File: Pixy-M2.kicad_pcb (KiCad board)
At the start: 4 copper layers, 66 x 100 mm, 78 parts, among them J1 USB_C_Receptacle_USB2.0_14P, J10 SM09B-SRSS-TB, J11 SM06B-SRSS-TB, J4 SM06B-SRSS-TB, J5 SM06B-SRSS-TB, J6 SM06B-SRSS-TB, J7 SM06B-SRSS-TB, J8 SM06B-SRSS-TB, J9 SM06B-SRSS-TB, Q1 AO4407A, SW1 SW_Push, SW2 SW_Push, SW3 JS102011SAQN, U1 ESP32-S3-WROOM-1-N16, U2 USBLC6-2SC6, U3 AP63203WU, U4 DRV8231ADSG, U5 DRV8231ADSG

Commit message: silkscreen: mark the battery bay and its lead route
B.SilkS now shows where the pack goes:
- its 62 x 17 mm outline between the motors, labelled with the part
  and "62 x 17 face on board, hook-and-loop";
- an arrow at the +X end where the XT30 and balance leads leave;
- the lead route as a dashed line forward and across the front strip,
  ending in an arrow at the left edge beside BT1's pins.

Each motor's "Pololu HP 6V N20" label used to sit in the inboard
encoder allowance, which is now inside the battery outline. The labels
move to the outboard allowance, and "ENC CONN SIDE" marks the face the
encoder board stands proud of.

battery_bay.py prints the battery marks, and assembly_marks.py draws the
motor labels in their new place. Run standalone, battery_bay.py moves
the labels on an already-marked board. A full rework.py regeneration
reproduces the board item for item. DRC is 0 violations, 0 unconnected
and 0 parity issues. The aperture audit passes. docs/images/
pcb-3d-bottom.png is re-rendered.

Co-Authored-By: Claude Opus 5.5 <noreply@anthropic.com>
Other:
- board text added: "62 x 17 face on board, hook-and-loop"
- board text added: "BATTERY 2S LiPo 450 mAh"
- board text added: "ENC CONN SIDE"
- board text added: "XT30 + balance leads"
- board text added: "XT30 LEAD: ROUND LEFT EDGE TO BT1 (TOP)"
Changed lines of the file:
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@@
 	)
 	(gr_line
+		(start 100.5 117.5)
+		(end 162.5 117.5)
+		(stroke
+			(width 0.15)
+			(type solid)
+		)
+		(layer "B.SilkS")
+	)
+	(gr_line
+		(start 100.5 134.5)
+		(end 100.5 117.5)
+		(stroke
+			(width 0.15)
+			(type solid)
+		)
+		(layer "B.SilkS")
+	)
+	(gr_line
+		(start 100.8 89.5)
+		(end 101.4928 89.1)
+		(stroke
+			(width 0.15)
+			(type solid)
+		)
+		(layer "B.SilkS")
+	)
+	(gr_line
+		(start 100.8 89.5)
+		(end 101.4928 89.9)
+		(stroke
+			(width 0.15)
+			(type solid)
+		)
+		(layer "B.SilkS")
+	)
+	(gr_line
 		(start 100.8 112.5)
 		(end 101.4928 112.1)
@@
 	)
 	(gr_line
+		(start 102.8 89.5)
+		(end 100.8 89.5)
+		(stroke
+			(width 0.15)
+			(type solid)
+		)
+		(layer "B.SilkS")
+	)
+	(gr_line
 		(start 106 112.5)
 		(end 100.8 112.5)
@@
 	)
 	(gr_line
+		(start 156 126)
+		(end 162.2 126)
+		(stroke
+			(width 0.15)
+			(type solid)
+		)
+		(layer "B.SilkS")
+	)
+	(gr_line
 		(start 157 136)
 		(end 157 148)
@@
 	)
 	(gr_line
+		(start 162.2 126)
+		(end 161.5072 125.6)
+		(stroke
+			(width 0.15)
+			(type solid)
+		)
+		(layer "B.SilkS")
+	)
+	(gr_line
+		(start 162.2 126)
+		(end 161.5072 126.4)
+		(stroke
+			(width 0.15)
+			(type solid)
+		)
+		(layer "B.SilkS")
+	)
+	(gr_line
+		(start 162.5 117.5)
+		(end 162.5 134.5)
+		(stroke
+			(width 0.15)
+			(type solid)
+		)
+		(layer "B.SilkS")
+	)
+	(gr_line
+		(start 162.5 126)
+		(end 164.5 124)
+		(stroke
+			(width 0.15)
+			(type dash)
+		)
+		(layer "B.SilkS")
+	)
+	(gr_line
+		(start 162.5 134.5)
+		(end 100.5 134.5)
+		(stroke
+			(width 0.15)
+			(type solid)
+		)
+		(layer "B.SilkS")
+	)
+	(gr_line
+		(start 164.5 89.5)
+		(end 100.8 89.5)
+		(stroke
+			(width 0.15)
+			(type dash)
+		)
+		(layer "B.SilkS")
+	)
+	(gr_line
+		(start 164.5 124)
+		(end 164.5 89.5)
+		(stroke
+			(width 0.15)
+			(type dash)
+		)
+		(layer "B.SilkS")
+	)
+	(gr_line
 		(start 165.2 144.5)
 		(end 164.5072 144.1)
@@
 	)
 	(gr_text "Pololu HP 6V N20"
-		(at 116 118 0)
+		(at 112 102 0)
 		(layer "B.SilkS")
 		(effects
@@
 		)
 	)
+	(gr_text "ENC CONN SIDE"
+		(at 128 102 0)
+		(layer "B.SilkS")
+		(effects
+			(font
+				(size 1 1)
+				(thickness 0.15)
+			)
+			(justify mirror)
+		)
+	)
 	(gr_text "ENC"
 		(at 128 110 0)
@@
 		)
 	)
+	(gr_text "BATTERY  2S LiPo 450 mAh"
+		(at 131.5 121 0)
+		(layer "B.SilkS")
+		(effects
+			(font
+				(size 1 1)
+				(thickness 0.15)
+			)
+			(justify mirror)
+		)
+	)
+	(gr_text "62 x 17 face on board, hook-and-loop"
+		(at 131.5 123.5 0)
+		(layer "B.SilkS")
+		(effects
+			(font
+				(size 1 1)
+				(thickness 0.15)
+			)
+			(justify mirror)
+		)
+	)
+	(gr_text "XT30 LEAD: ROUND LEFT EDGE TO BT1 (TOP)"
+		(at 132 88 0)
+		(layer "B.SilkS")
+		(effects
+			(font
+				(size 1 1)
+				(thickness 0.15)
+			)
+			(justify mirror)
+		)
+	)
 	(gr_text "ENC"
 		(at 138 142 0)
@@
 		)
 	)
+	(gr_text "ENC CONN SIDE"
+		(at 138 150 0)
+		(layer "B.SilkS")
+		(effects
+			(font
+				(size 1 1)
+				(thickness 0.15)
+			)
+			(justify mirror)
+		)
+	)
 	(gr_text "MOTOR B"
 		(at 149.5 140.5 0)
@@
 		)
 	)
+	(gr_text "XT30 + balance leads"
+		(at 151 128.5 0)
+		(layer "B.SilkS")
+		(effects
+			(font
+				(size 1 1)
+				(thickness 0.15)
+			)
+			(justify mirror)
+		)
+	)
 	(gr_text "Pololu HP 6V N20"
-		(at 150 134 0)
+		(at 154 150 0)
 		(layer "B.SilkS")
 		(effects
@@
 	(group "MOTOR A left"
 		(members "182aea95-9cac-46fa-9891-7ba377806479" "2f65c22c-14ae-4f42-a709-9b8d5caaa5b2"
-			"724801b8-62fc-4983-98b0-ae9173e109c6" "731f0e17-fc26-4354-be69-66f241ecec50"
-			"78fb0ae1-b412-4b57-b170-880f7e821dcf" "8c104fb5-1e0c-45c4-922a-1d16e56ce52a"
-			"932dff99-57df-49bd-b39b-bcbb18650a0f" "96fded54-0e83-4a2c-af15-2bd8b529ef9e"
-			"9f73eaea-9302-4c33-ad8d-0effa9570fa8" "9fbd5650-8a3e-4572-a359-2861bb6658ff"
-			"a19da8c7-bf97-4091-8b3c-38a013214ff2" "b732a7a5-04e5-43d0-b666-8b87410bfe6f"
-			"b8f2ee2f-2cc3-4c76-8a9d-eeb49646817c" "ef057167-08ec-4e79-9cf7-0bf9724b438e"
+			"53c676fe-a335-40a2-9a87-d7526bc6f8c1" "724801b8-62fc-4983-98b0-ae9173e109c6"
+			"731f0e17-fc26-4354-be69-66f241ecec50" "78fb0ae1-b412-4b57-b170-880f7e821dcf"
+			"8c104fb5-1e0c-45c4-922a-1d16e56ce52a" "932dff99-57df-49bd-b39b-bcbb18650a0f"
+			"96fded54-0e83-4a2c-af15-2bd8b529ef9e" "9f73eaea-9302-4c33-ad8d-0effa9570fa8"
+			"9fbd5650-8a3e-4572-a359-2861bb6658ff" "a19da8c7-bf97-4091-8b3c-38a013214ff2"
+			"b732a7a5-04e5-43d0-b666-8b87410bfe6f" "b8f2ee2f-2cc3-4c76-8a9d-eeb49646817c"
+			"ef057167-08ec-4e79-9cf7-0bf9724b438e"
 		)
 	)
 	(group "MOTOR B right"
 		(members "0f1f0ffd-d82d-4e67-a17a-63341daef4a0" "0fdc3546-4d59-47d1-8cc6-e377abaa7ab5"
-			"4a79a600-30c0-4714-a8a7-72aed6312c1c" "7daca688-97f0-4970-939d-d535cb80d69c"
-			"8e764ac1-cf16-446e-a34d-87ffc74df771" "a9721b52-0e68-417a-8dd7-89f1f280f427"
-			"ad33dd5f-4225-4708-816f-030241213b0d" "b8e69d41-da5b-42cb-b5ad-6211be34cdf2"
-			"bcda8ce7-7330-4a6e-ad1a-35d33d416d2b" "d6442bf3-5cec-4718-aa87-49ee13f4cb53"
-			"d6f641c7-7735-4c2b-8e4d-9783522e7b47" "efc585e6-88f0-4ecc-bb5d-9bfebf6fc967"
-			"f00c8229-d97d-464d-8c04-33f36ac6bb3d" "f21dc9e0-eb5e-45dd-a607-3d5a687f84eb"
+			"4912f350-1b29-4300-95c6-d19ba006e40e" "4a79a600-30c0-4714-a8a7-72aed6312c1c"
+			"7daca688-97f0-4970-939d-d535cb80d69c" "8e764ac1-cf16-446e-a34d-87ffc74df771"
+			"a9721b52-0e68-417a-8dd7-89f1f280f427" "ad33dd5f-4225-4708-816f-030241213b0d"
+			"b8e69d41-da5b-42cb-b5ad-6211be34cdf2" "bcda8ce7-7330-4a6e-ad1a-35d33d416d2b"
+			"d6442bf3-5cec-4718-aa87-49ee13f4cb53" "d6f641c7-7735-4c2b-8e4d-9783522e7b47"
+			"efc585e6-88f0-4ecc-bb5d-9bfebf6fc967" "f00c8229-d97d-464d-8c04-33f36ac6bb3d"
+			"f21dc9e0-eb5e-45dd-a607-3d5a687f84eb"
+		)
+	)
+	(group "Battery 2S LiPo"
+		(members "1f756f54-700a-4b72-8c48-fb78f77be5c2" "2bf49ae5-ad71-47fd-bcae-bb4a34affefd"
+			"2e12e2d9-c110-41b5-a665-7e36aaf4e661" "30fa4877-ac52-4ba0-802d-24a011503e21"
+			"42349a8b-0c73-4b39-a33c-f898558e7e66" "58017f5e-8cc7-438d-83ad-afd2513fb6b0"
+			"5a2f327a-d665-4a46-a37a-faead681c1b4" "67de89d8-07e8-459d-9cf0-97794442ad0c"
+			"705298cb-41fb-4b0a-b5c3-0a6fb6671598" "70fec421-3e8d-4c27-af04-3baa416c8687"
+			"8010a8b4-c589-4faa-9333-068803a2f652" "92ea9e6d-a648-4d3e-b0e9-235c1ea28ac4"
+			"a3650a10-ee04-4e65-a642-60867b826b2a" "b819c550-9660-4e89-8e2f-7ab50507bc72"
+			"e30f7bb5-e967-4b4e-8e8a-673eae03dd72" "ead91f8e-c96c-49e1-886a-5d0ad5f9b5c2"
+			"efb92332-e236-4b47-93ee-39151fe97e23"
 		)
 	)

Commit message: layout: move R8/C13 beside U3.2 and take REG_EN out from under U3
REG_EN is a ~20 kOhm node 1.2 V above the EN comparator threshold, and
the layout rule was to put R8 and C13 next to U3.2. The issue-5 FB trace
ran down U3's west side, so EN could only leave through a via under the
package, 0.40 mm from the SW pin. R8 and C13 sat 7.35 and 9.9 mm of
copper away.

C13 and R8 now stand in a row just west of U3, and EN -> C13.1 -> R8.1
is one straight top-layer run (1.91 / 3.66 mm of copper). FB keeps its
via-free top-layer sense to C11 and turns south round the outside of the
new parts. A via on FB would bond it to the In2 3V3 pour beside U3,
which is what review finding 5 removed. REG_EN's long leg crosses under
FB on B.Cu instead; both of its vias are 5.65 mm or more from switching
copper. The VSYS hop's upper via moves north of FB. New vias keep their
In1/In2 antipads separate.

REG_EN's closest approach to SW/BST is now U3's own 0.95 mm pin gap, and
the "REG_EN clear of the switch node" floor goes from 0.35 to 0.9 mm. It
fires on the old board and on a copy with REG_EN copper under U3.

tools/autoroute/reg_en.py does this, and rework.py runs it last. A full
rework.py regeneration reproduces the board item for item. DRC is 0
violations, 0 unconnected and 0 parity issues; the aperture audit passes
with 253 vias. Evidence is in layout/reg-en/.

Also corrects issue 5's note that FB stays 2.1 mm from SW/BST: it passes
TP4 at 1.35 mm, before and after this change. docs/images/pcb-3d-top.png
and pcb-copper-top.png are re-rendered; pcb-3d-iso.png is not, since its
camera settings are not recorded.

Co-Authored-By: Claude Opus 5.5 <noreply@anthropic.com>
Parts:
- moved C13 6.06 mm to (136.2, 97.0), turned to -90 degrees
- moved R8 4.03 mm to (134.5, 97.2), turned to -90 degrees
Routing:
- net /ESP_3V3: track 93.8 -> 102.0 mm
- net /REG_EN: track 17.7 -> 14.3 mm
- net /VSYS: track 37.2 -> 37.8 mm
- net GND: track 114.9 -> 115.4 mm

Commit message: layout: keep the IPROPI sense runs clear of motor and drive copper
GPIO2 and GPIO10 carry each DRV8231A's IPROPI output (1500 uA/A into
2.2 kOhm) to the ADC. They came within 0.70 mm (GPIO2, MOT_A_1 at J8) and
0.53 mm (GPIO10, MOT_A_2) of motor copper, and ran long stretches beside
their own driver's IN1/IN2. The cause was where the sense resistors sat:

- R17 was east of U4's IN1/IN2 escapes, so GPIO2 hopped over them on
  B.Cu over the In2 VBAT island. But the three nets leave U4 in the order
  they reach U1's west column, so nothing else needed that crossing.
- R18 was west of U5's stacked GPIO41/42 pair, so GPIO10 ran down the
  channel beside MOT_A_2, then 8 mm beside GPIO42 on B.Cu at 0.25 mm.

R17 moves west of the escapes and GPIO2 runs down beside it, 1.7 mm from
MOT_A_1, with no via. R18 moves east of the pair. GPIO10 crosses the pair
once, under U5's own pins, then rises to R18 and rejoins its old diagonal
to U1 past the island. The channel beside MOT_A_2 is left empty.

GPIO2/GPIO10 now come no closer than 1.30 / 0.80 mm to motor copper: U4's
own pin 1 to pin 8, and GPIO10's escape via. No other stretch is within
1 mm. Track within 0.6 mm of a drive line falls from 6.8 / 13.7 mm to
3.7 / 5.6 mm. The "IPROPI clear of motor outputs" floor goes from 0.25
to 0.75 mm, and fires on the old board and on a broken copy.

tools/autoroute/ipropi.py does this, and rework.py runs it after
reg_en.py. A full rework.py regeneration reproduces the board item for
item. DRC is 0 violations, 0 unconnected and 0 parity issues, and ERC is
0. The aperture audit passes with 254 vias. Evidence is in layout/ipropi/.

The README item now asks only for the hardware check. TI's remedy for
early current-limit trips, 10 nF on IPROPI, can be stacked on R17/R18.
The firmware notes add that IPROPI reads nothing in coast.
docs/images/pcb-3d-top.png and pcb-copper-top.png are re-rendered.

Co-Authored-By: Claude Opus 5.5 <noreply@anthropic.com>
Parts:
- moved R17 5.05 mm to (104.5, 120.3), turned to 90 degrees
- moved R18 2.57 mm to (118.5, 118.6), turned to 180 degrees
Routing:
- net /GPIO10: track 42.7 -> 38.6 mm, vias 2 -> 4
- net /GPIO2: track 53.5 -> 51.6 mm, vias 2 -> 0
- net GND: track 115.4 -> 115.6 mm, vias 88 -> 89

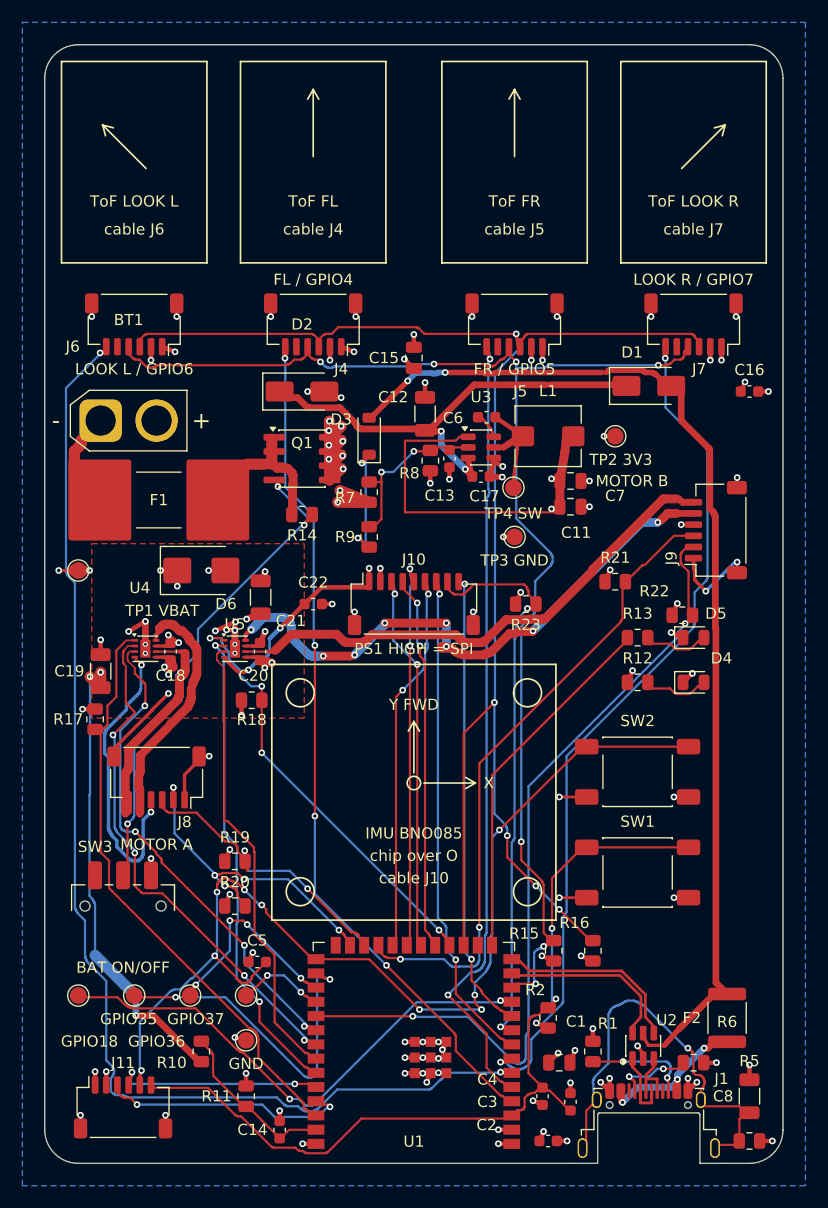
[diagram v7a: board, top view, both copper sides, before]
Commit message: U1: plug-in ESP32-S3-DevKitC-1-N8R8 on SMD sockets, same 66 x 100 mm board
Replace the soldered WROOM-1 module with an Espressif ESP32-S3-DevKitC-1-N8R8
(v1.1) on two 1x22 2.54 mm SMD female headers, and remove what the devkit
carries itself. The outline stays 66 x 100 mm for the diagonal runs.

Schematic (tools/schematic/devkit.py):
- U1 -> PCM_Espressif:ESP32-S3-DevKitC on Pixy-M2:ESP32-S3-DevKitC-1_SMD_Sockets;
  Value, Footprint, Datasheet and MPN changed together.
- 21 parts removed: the USB-C input (J1, U2, F2, R1, R5, R6, C8), the USB
  supply path (D1, D3, R9), reset/boot (R2, C3-C5, SW1, SW2), J11 and TP5-TP8.
- The AP63203 feeds the devkit's 3V3 pins; its 5V pin is unused.
- Encoder B OUT B moves from GPIO38 (the v1.1 RGB LED) to GPIO18.
- 13 no-connect flags on the pins the devkit uses itself. 59 nets, 57 parts,
  ERC 0/0.

Layout (tools/autoroute/devkit.py, new rework stage 20):
- U1 along the right edge, antenna over the rear edge, USB end to the front.
- The IMU moves into the 25 mm column beside the devkit (8.6 mm left of and
  7.5 mm behind the rotation centre). J10/C22 go behind it, J8/SW3 clear of
  it, J9 in front of the devkit, the LEDs to the rear-left corner and the
  sense chain against GPIO1.
- Rips and re-routes every affected net, keeping the hand-placed motor-corner,
  buck, FB and REG_EN copper. A* respects the custom clearance floors. The
  stage ends with KiCad-style dead-end pruning, removal of via-only GND stubs
  and one GND via per B.Cu pour island.
- Closes J1's outline notch and moves the antenna keep-out.
- Footprint generator: tools/autoroute/devkit_footprint.py.
- DRC 0 violations / 0 unconnected / 0 parity. Aperture audit passes with
  192 vias (254 on main). A full rework.py replay reproduces the board.
- Measurements are in layout/devkit/. Motor loops: A 26.4 mm², B 27.8 mm²
  (main 23.9 / 9.8, where B's opposite lobes nearly cancelled).

Rules: USB rules and netclass removed; Hole clearance 0.30 mm everywhere.
via_openings.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
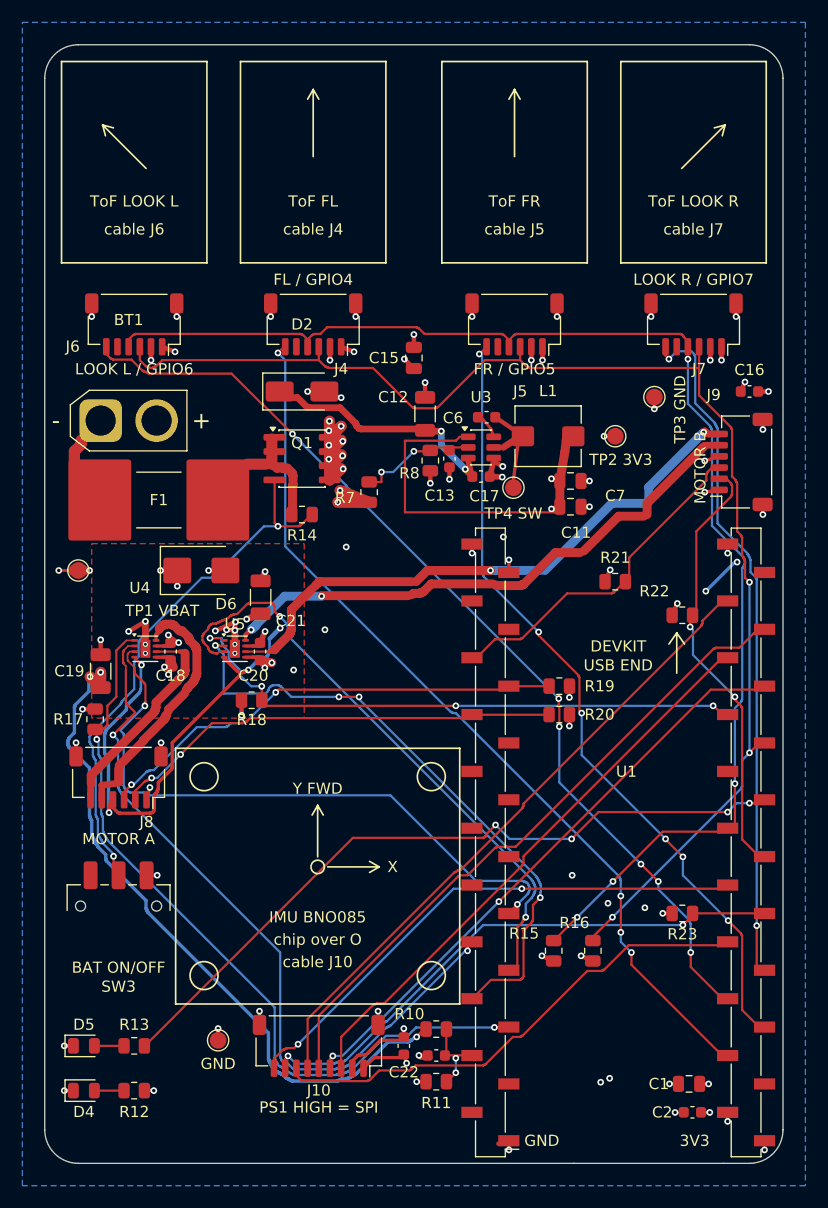
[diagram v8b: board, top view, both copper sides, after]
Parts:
- removed C3: 1uF 16V, Capacitor_SMD:C_0603_1608Metric
- removed C4, C5: 0.1uF 16V, Capacitor_SMD:C_0603_1608Metric
- removed C8: 4.7nF 1kV, Capacitor_SMD:C_1206_3216Metric
- removed D1: MBRA340T3G, Diode_SMD:D_SMA
- removed D3: BAT54W, Diode_SMD:D_SOD-123
- removed F2: 500mA 15V, Fuse:Fuse_1812_4532Metric
- removed J1: USB_C_Receptacle_USB2.0_14P, Connector_USB:USB_C_Receptacle_Amphenol_12401948E412A
- removed J11: SM06B-SRSS-TB, Connector_JST:JST_SH_SM06B-SRSS-TB_1x06-1MP_P1.00mm_Horizontal
- removed R1, R6: 5.1kOhm, Resistor_SMD:R_0805_2012Metric
- removed R2: 10kOhm, Resistor_SMD:R_0805_2012Metric
- removed R5: 1MOhm, Resistor_SMD:R_0805_2012Metric
- removed R9: 39kOhm 1%, Resistor_SMD:R_0805_2012Metric
- removed SW1, SW2: SW_Push, Button_Switch_SMD:SW_Push_1P1T_NO_E-Switch_TL3301NxxxxxG
- removed TP5: GPIO18, TestPoint:TestPoint_Pad_D1.5mm
- removed TP6: GPIO35, TestPoint:TestPoint_Pad_D1.5mm
- removed TP7: GPIO36, TestPoint:TestPoint_Pad_D1.5mm
- removed TP8: GPIO37, TestPoint:TestPoint_Pad_D1.5mm
- removed U2: USBLC6-2SC6, Package_TO_SOT_SMD:SOT-23-6
- U1: value ESP32-S3-WROOM-1-N16 -> ESP32-S3-DevKitC-1-N8R8; footprint Pixy-M2:ESP32-S3-WROOM-1_AntennaOverhang -> Pixy-M2:ESP32-S3-DevKitC-1_SMD_Sockets
- moved D4 65.6 mm to (103.5, 153.5)
- moved D5 65.6 mm to (103.5, 149.5)
- moved R12 57.9 mm to (108.0, 153.5), turned to 180 degrees
- moved R13 57.9 mm to (108.0, 149.5), turned to 180 degrees
- moved J10 40.4 mm to (124.5, 149.5), turned to 180 degrees
- moved C22 40.3 mm to (132.1, 149.5), turned to 90 degrees
- moved R20 33.7 mm to (146.0, 119.9), turned to 180 degrees
- moved R19 33.0 mm to (146.0, 117.3), turned to 180 degrees
- moved R23 31.0 mm to (157.0, 137.7)
- moved U1 30.8 mm to (162.7, 158.0)
- moved R10 21.1 mm to (135.0, 148.0), turned to 0 degrees
- moved TP3 17.7 mm to (154.5, 91.5)
- moved R11 17.0 mm to (135.0, 152.7), turned to 180 degrees
- moved C14 15.5 mm to (135.0, 150.4), turned to 180 degrees
- moved C2 13.2 mm to (157.9, 155.4), turned to 180 degrees
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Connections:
- J9 pad 2: /GPIO38 -> /GPIO18
- R22 pad 2: /GPIO38 -> /GPIO18
- U1 pad 1: GND -> /ESP_3V3
- U1 pad 13: /USB_D- -> /GPIO3
- U1 pad 14: /USB_D+ -> unconnected-(U1-GPIO46-Pad14)
- U1 pad 15: /GPIO3 -> /GPIO9
- U1 pad 16: unconnected-(U1-GPIO46-Pad16) -> /GPIO10
- U1 pad 17: /GPIO9 -> /GPIO11
- U1 pad 18: /GPIO10 -> /GPIO12
- U1 pad 19: /GPIO11 -> /GPIO13
- U1 pad 20: /GPIO12 -> /GPIO14
- U1 pad 21: /GPIO13 -> unconnected-(U1-5V-Pad21)
- U1 pad 22: /GPIO14 -> GND
- U1 pad 23: /GPIO21 -> GND
- U1 pad 24: /GPIO47 -> GND
- U1 pad 25: /GPIO48 -> unconnected-(U1-GPIO19/USB_D--Pad25)
- U1 pad 27: /GPIO0 -> /GPIO21
- U1 pad 28: /GPIO35 -> /GPIO47
- U1 pad 29: /GPIO36 -> /GPIO48
- U1 pad 3: /CHIP_PU -> unconnected-(U1-CHIP_PU-Pad3)
- U1 pad 30: /GPIO37 -> unconnected-(U1-GPIO45-Pad30)
- U1 pad 31: /GPIO38 -> unconnected-(U1-GPIO0-Pad31)
- U1 pad 32: /GPIO39 -> unconnected-(U1-GPIO35-Pad32)
- U1 pad 33: /GPIO40 -> unconnected-(U1-GPIO36-Pad33)
- U1 pad 34: /GPIO41 -> unconnected-(U1-GPIO37-Pad34)
- U1 pad 35: /GPIO42 -> unconnected-(U1-GPIO38-Pad35)
- U1 pad 36: /GPIO44 -> /GPIO39
- U1 pad 37: /GPIO43 -> /GPIO40
- U1 pad 38: /GPIO2 -> /GPIO41
- U1 pad 39: /VBAT_SENSE -> /GPIO42
- U1 pad 40: GND -> /GPIO2
- U1 pad 41: GND -> /VBAT_SENSE
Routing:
- net /VBUS: track 90.4 -> 0.00 mm, vias 2 -> 0
- net /GPIO0: track 89.8 -> 0.00 mm, vias 9 -> 0
- net /GPIO38: track 71.7 -> 0.00 mm, vias 2 -> 0
- net /CHIP_PU: track 71.4 -> 0.00 mm, vias 2 -> 0
- net GND: track 115.6 -> 75.9 mm, vias 89 -> 72
- net /GPIO3: track 31.2 -> 64.3 mm, vias 0 -> 4
- net Net-(J1-SHIELD): track 32.3 -> 0.00 mm, vias 1 -> 0
- net /GPIO35: track 30.0 -> 0.00 mm, vias 2 -> 0
- net /GPIO21: track 55.0 -> 27.9 mm, vias 2 -> 0
- net /GPIO13: track 34.6 -> 57.3 mm, vias 2 -> 0
- net /GPIO6: track 107.5 -> 85.7 mm, vias 2 -> 6
- net /GPIO14: track 34.6 -> 56.3 mm, vias 2 -> 0
- net /GPIO43: track 21.1 -> 0.00 mm, vias 2 -> 0
- net /GPIO40: track 46.3 -> 66.9 mm, vias 4 -> 2
- net /VBAT: track 77.6 -> 97.9 mm
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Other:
- board text removed: "GPIO18"
- board text removed: "GPIO35"
- board text removed: "GPIO36"
- board text removed: "GPIO37"
